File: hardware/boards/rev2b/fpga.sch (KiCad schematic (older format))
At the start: 71 parts, among them J1 SD_Card, J6 Conn_02x08_Odd_Even, Q1 DNP(RE1C002UN), SW1 SW_PUSH, U6 XC7A15T-FTG256, U7 MX25L3233F

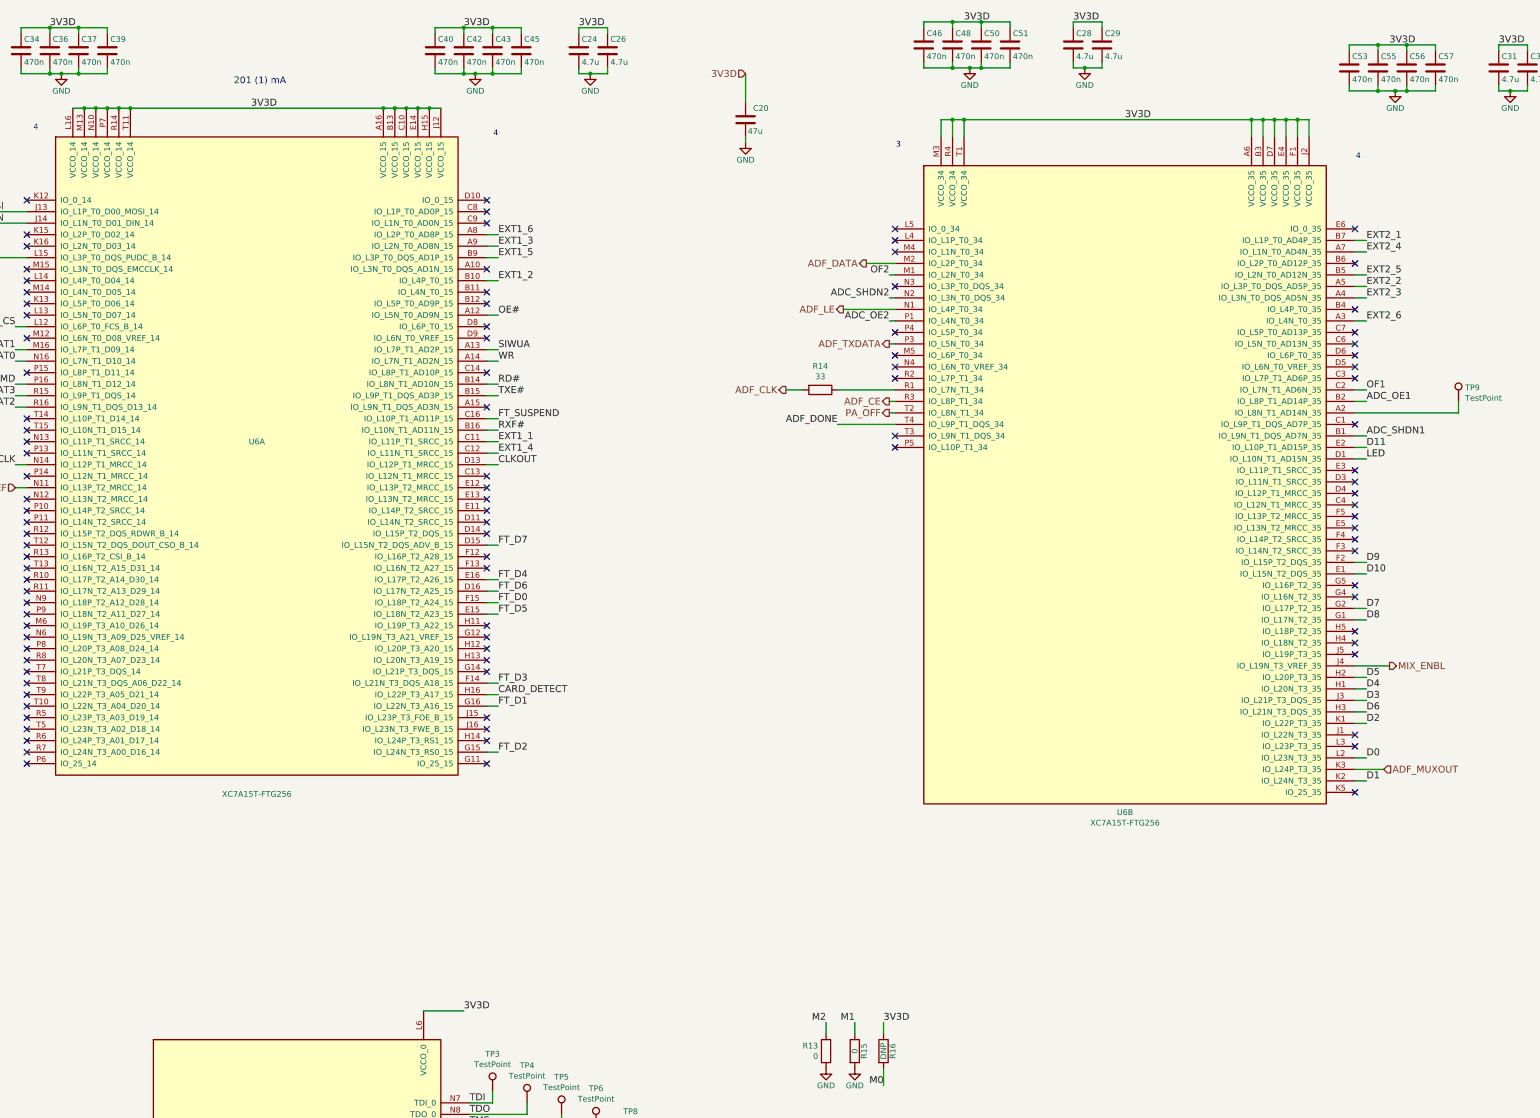
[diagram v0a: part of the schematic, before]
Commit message: rev2 pcb: finish routing traces
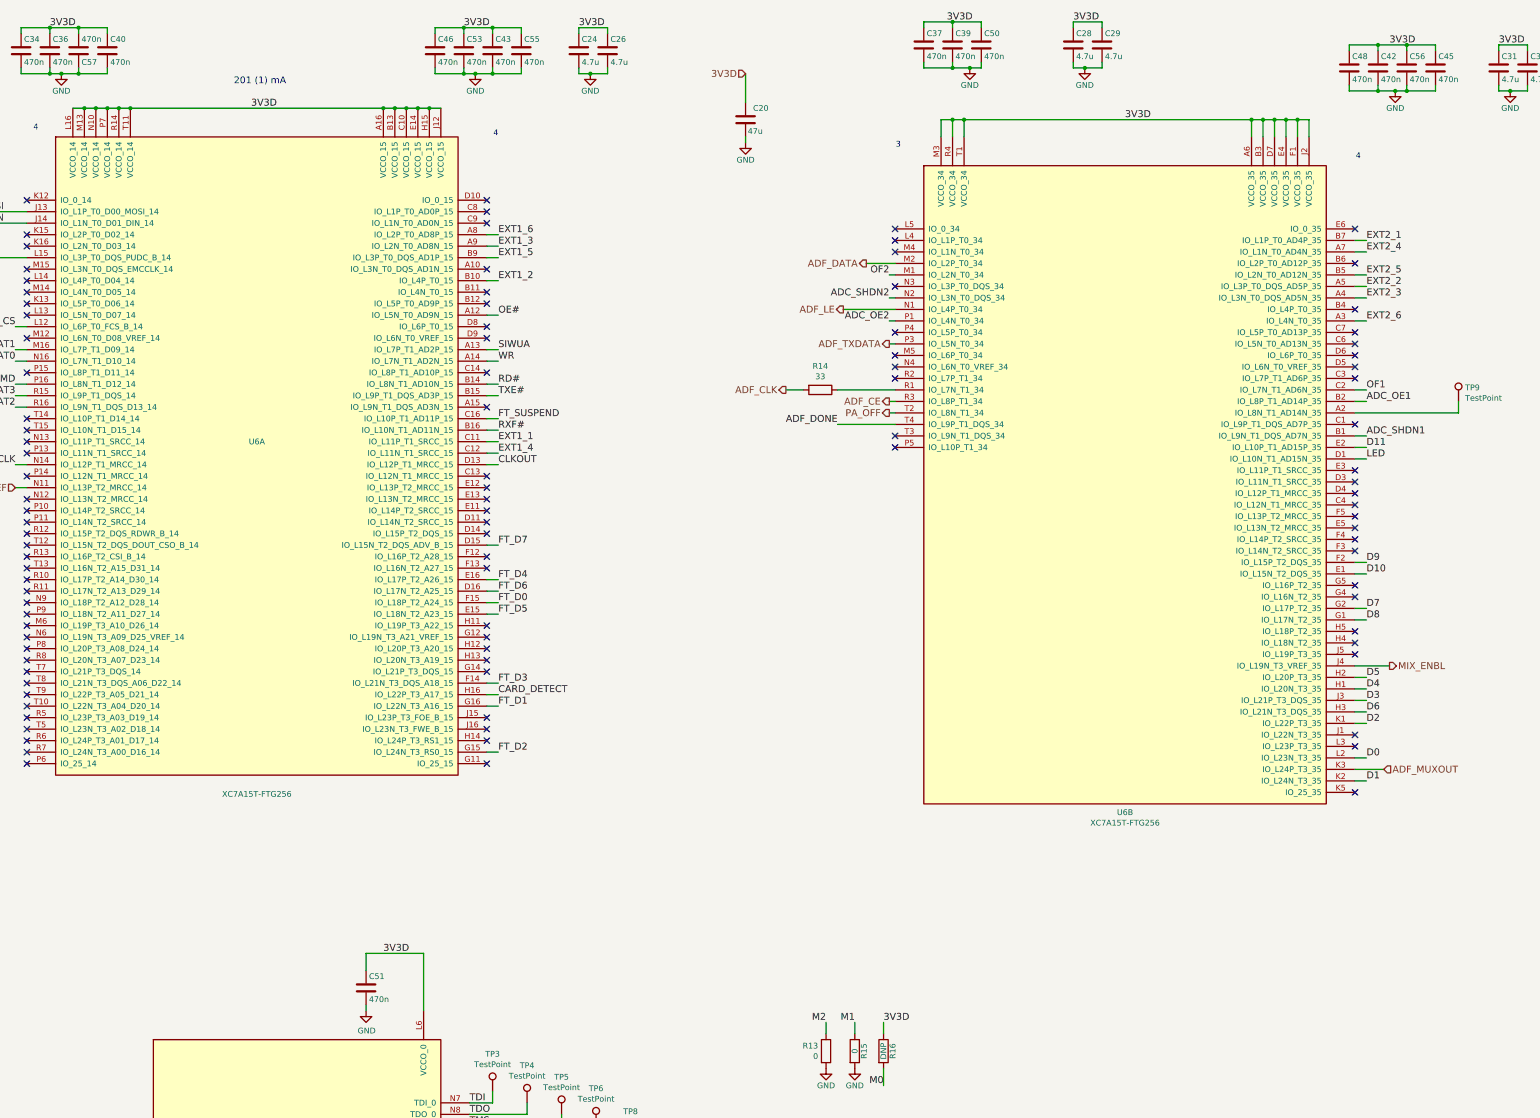
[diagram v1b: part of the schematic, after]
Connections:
- net 3V3D: now also C57.2; no longer C57.1
- net GND: now also C57.1; no longer C57.2
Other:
- moved on the sheet: C37, C39, C40, C42, C45, C46, C48, C51, C53, C55, C57
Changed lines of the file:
@@
 Connection ~ 19650 11900
 Connection ~ 16300 950
-Connection ~ 16550 950
 Connection ~ 20000 1150
 Connection ~ 20250 1150
 Connection ~ 20250 1550
 Connection ~ 20000 1550
-Connection ~ 16550 1350
 Connection ~ 16300 1350
 Connection ~ 7250 15300
@@
 	11150 14150 11150 14200
 Wire Wire Line
-	11700 9550 12050 9550
-Wire Wire Line
 	11800 1000 11800 1050
 Wire Wire Line
@@
 Wire Wire Line
 	16550 1350 16450 1350
-Wire Wire Line
-	16800 950  16550 950
-Wire Wire Line
-	16800 1000 16800 950
-Wire Wire Line
-	16800 1300 16800 1350
-Wire Wire Line
-	16800 1350 16550 1350
 Wire Wire Line
 	16850 11450 16850 11500
@@
 Text Label 12050 1000 0    60   ~ 0
 3V3D
-Text Label 12050 9550 0    60   ~ 0
+Text Label 11350 9050 0    60   ~ 0
 3V3D
 Text Label 12100 10350 0    60   ~ 0
@@
 Text Label 15750 3550 2    60   ~ 0
 ADC_OE2
-Text Label 16400 950  0    60   ~ 0
+Text Label 16250 950  0    60   ~ 0
 3V3D
 Text Label 16850 11450 0    60   ~ 0
@@
 L Device:C C37
 U 1 1 584FBF7D
-P 8700 1200
-F 0 "C37" H 8725 1300 50  0000 L CNN
-F 1 "470n" H 8725 1100 50  0000 L CNN
-F 2 "Capacitor_SMD:C_0603_1608Metric" H 8738 1050 30  0001 C CNN
-F 3 "" H 8700 1200 60  0000 C CNN
-F 4 "" H -3700 -6700 50  0001 C CNN "MFN"
-	1    8700 1200
+P 16050 1150
+F 0 "C37" H 16075 1250 50  0000 L CNN
+F 1 "470n" H 16075 1050 50  0000 L CNN
+F 2 "Capacitor_SMD:C_0603_1608Metric" H 16088 1000 30  0001 C CNN
+F 3 "" H 16050 1150 60  0000 C CNN
+F 4 "" H 3650 -6750 50  0001 C CNN "MFN"
+	1    16050 1150
 	1    0    0    -1
 $EndComp
@@
 L Device:C C39
 U 1 1 584FBE1F
-P 8950 1200
-F 0 "C39" H 8975 1300 50  0000 L CNN
-F 1 "470n" H 8975 1100 50  0000 L CNN
-F 2 "Capacitor_SMD:C_0603_1608Metric" H 8988 1050 30  0001 C CNN
-F 3 "" H 8950 1200 60  0000 C CNN
-F 4 "" H -3700 -6700 50  0001 C CNN "MFN"
-	1    8950 1200
+P 16300 1150
+F 0 "C39" H 16325 1250 50  0000 L CNN
+F 1 "470n" H 16325 1050 50  0000 L CNN
+F 2 "Capacitor_SMD:C_0603_1608Metric" H 16338 1000 30  0001 C CNN
+F 3 "" H 16300 1150 60  0000 C CNN
+F 4 "" H 3650 -6750 50  0001 C CNN "MFN"
+	1    16300 1150
 	1    0    0    -1
 $EndComp
@@
 L Device:C C40
 U 1 1 584FBCC6
-P 11800 1200
-F 0 "C40" H 11825 1300 50  0000 L CNN
-F 1 "470n" H 11825 1100 50  0000 L CNN
-F 2 "Capacitor_SMD:C_0603_1608Metric" H 11838 1050 30  0001 C CNN
-F 3 "" H 11800 1200 60  0000 C CNN
-F 4 "" H -1100 -6700 50  0001 C CNN "MFN"
-	1    11800 1200
+P 8950 1200
+F 0 "C40" H 8975 1300 50  0000 L CNN
+F 1 "470n" H 8975 1100 50  0000 L CNN
+F 2 "Capacitor_SMD:C_0603_1608Metric" H 8988 1050 30  0001 C CNN
+F 3 "" H 8950 1200 60  0000 C CNN
+F 4 "" H -3950 -6700 50  0001 C CNN "MFN"
+	1    8950 1200
 	1    0    0    -1
 $EndComp
@@
 L Device:C C42
 U 1 1 584FBB6A
-P 12050 1200
-F 0 "C42" H 12075 1300 50  0000 L CNN
-F 1 "470n" H 12075 1100 50  0000 L CNN
-F 2 "Capacitor_SMD:C_0603_1608Metric" H 12088 1050 30  0001 C CNN
-F 3 "" H 12050 1200 60  0000 C CNN
-F 4 "" H -1100 -6700 50  0001 C CNN "MFN"
-	1    12050 1200
+P 20000 1350
+F 0 "C42" H 20025 1450 50  0000 L CNN
+F 1 "470n" H 20025 1250 50  0000 L CNN
+F 2 "Capacitor_SMD:C_0603_1608Metric" H 20038 1200 30  0001 C CNN
+F 3 "" H 20000 1350 60  0000 C CNN
+F 4 "" H 6850 -6550 50  0001 C CNN "MFN"
+	1    20000 1350
 	1    0    0    -1
 $EndComp
@@
 L Device:C C45
 U 1 1 583B1CF1
-P 12550 1200
-F 0 "C45" H 12575 1300 50  0000 L CNN
-F 1 "470n" H 12575 1100 50  0000 L CNN
-F 2 "Capacitor_SMD:C_0603_1608Metric" H 12588 1050 30  0001 C CNN
-F 3 "" H 12550 1200 60  0000 C CNN
-F 4 "" H -1100 -6700 50  0001 C CNN "MFN"
-	1    12550 1200
+P 20500 1350
+F 0 "C45" H 20525 1450 50  0000 L CNN
+F 1 "470n" H 20525 1250 50  0000 L CNN
+F 2 "Capacitor_SMD:C_0603_1608Metric" H 20538 1200 30  0001 C CNN
+F 3 "" H 20500 1350 60  0000 C CNN
+F 4 "" H 6850 -6550 50  0001 C CNN "MFN"
+	1    20500 1350
 	1    0    0    -1
 $EndComp
@@
 L Device:C C46
 U 1 1 58531E80
-P 16050 1150
-F 0 "C46" H 16075 1250 50  0000 L CNN
-F 1 "470n" H 16075 1050 50  0000 L CNN
-F 2 "Capacitor_SMD:C_0603_1608Metric" H 16088 1000 30  0001 C CNN
-F 3 "" H 16050 1150 60  0000 C CNN
-F 4 "" H 2150 -6750 50  0001 C CNN "MFN"
-	1    16050 1150
+P 11800 1200
+F 0 "C46" H 11825 1300 50  0000 L CNN
+F 1 "470n" H 11825 1100 50  0000 L CNN
+F 2 "Capacitor_SMD:C_0603_1608Metric" H 11838 1050 30  0001 C CNN
+F 3 "" H 11800 1200 60  0000 C CNN
+F 4 "" H -2100 -6700 50  0001 C CNN "MFN"
+	1    11800 1200
 	1    0    0    -1
 $EndComp
@@
 L Device:C C48
 U 1 1 5C7E4CDC
-P 16300 1150
-F 0 "C48" H 16325 1250 50  0000 L CNN
-F 1 "470n" H 16325 1050 50  0000 L CNN
-F 2 "Capacitor_SMD:C_0603_1608Metric" H 16338 1000 30  0001 C CNN
-F 3 "" H 16300 1150 60  0000 C CNN
-F 4 "" H 2150 -6750 50  0001 C CNN "MFN"
-	1    16300 1150
+P 19750 1350
+F 0 "C48" H 19775 1450 50  0000 L CNN
+F 1 "470n" H 19775 1250 50  0000 L CNN
+F 2 "Capacitor_SMD:C_0603_1608Metric" H 19788 1200 30  0001 C CNN
+F 3 "" H 19750 1350 60  0000 C CNN
+F 4 "" H 5600 -6550 50  0001 C CNN "MFN"
+	1    19750 1350
 	1    0    0    -1
 $EndComp
@@
 L Device:C C51
 U 1 1 5C7E4E26
-P 16800 1150
-F 0 "C51" H 16825 1250 50  0000 L CNN
-F 1 "470n" H 16825 1050 50  0000 L CNN
-F 2 "Capacitor_SMD:C_0603_1608Metric" H 16838 1000 30  0001 C CNN
-F 3 "" H 16800 1150 60  0000 C CNN
-F 4 "" H 2150 -6750 50  0001 C CNN "MFN"
-	1    16800 1150
+P 11200 9350
+F 0 "C51" H 11225 9450 50  0000 L CNN
+F 1 "470n" H 11225 9250 50  0000 L CNN
+F 2 "Capacitor_SMD:C_0603_1608Metric" H 11238 9200 30  0001 C CNN
+F 3 "" H 11200 9350 60  0000 C CNN
+F 4 "" H -3450 1450 50  0001 C CNN "MFN"
+	1    11200 9350
 	1    0    0    -1
 $EndComp
@@
 L Device:C C53
 U 1 1 5C7E4ECC
-P 19750 1350
-F 0 "C53" H 19775 1450 50  0000 L CNN
-F 1 "470n" H 19775 1250 50  0000 L CNN
-F 2 "Capacitor_SMD:C_0603_1608Metric" H 19788 1200 30  0001 C CNN
-F 3 "" H 19750 1350 60  0000 C CNN
-F 4 "" H 4850 -6550 50  0001 C CNN "MFN"
-	1    19750 1350
+P 12050 1200
+F 0 "C53" H 12075 1300 50  0000 L CNN
+F 1 "470n" H 12075 1100 50  0000 L CNN
+F 2 "Capacitor_SMD:C_0603_1608Metric" H 12088 1050 30  0001 C CNN
+F 3 "" H 12050 1200 60  0000 C CNN
+F 4 "" H -2850 -6700 50  0001 C CNN "MFN"
+	1    12050 1200
 	1    0    0    -1
 $EndComp
@@
 L Device:C C55
 U 1 1 5C7E4F74
-P 20000 1350
-F 0 "C55" H 20025 1450 50  0000 L CNN
-F 1 "470n" H 20025 1250 50  0000 L CNN
-F 2 "Capacitor_SMD:C_0603_1608Metric" H 20038 1200 30  0001 C CNN
-F 3 "" H 20000 1350 60  0000 C CNN
-F 4 "" H 4850 -6550 50  0001 C CNN "MFN"
-	1    20000 1350
+P 12550 1200
+F 0 "C55" H 12575 1300 50  0000 L CNN
+F 1 "470n" H 12575 1100 50  0000 L CNN
+F 2 "Capacitor_SMD:C_0603_1608Metric" H 12588 1050 30  0001 C CNN
+F 3 "" H 12550 1200 60  0000 C CNN
+F 4 "" H -2600 -6700 50  0001 C CNN "MFN"
+	1    12550 1200
 	1    0    0    -1
 $EndComp
@@
 L Device:C C57
 U 1 1 5C7E50CE
-P 20500 1350
-F 0 "C57" H 20525 1450 50  0000 L CNN
-F 1 "470n" H 20525 1250 50  0000 L CNN
-F 2 "Capacitor_SMD:C_0603_1608Metric" H 20538 1200 30  0001 C CNN
-F 3 "" H 20500 1350 60  0000 C CNN
-F 4 "" H 4850 -6550 50  0001 C CNN "MFN"
-	1    20500 1350
-	1    0    0    -1
+P 8700 1200
+F 0 "C57" H 8725 1300 50  0000 L CNN
+F 1 "470n" H 8725 1100 50  0000 L CNN
+F 2 "Capacitor_SMD:C_0603_1608Metric" H 8738 1050 30  0001 C CNN
+F 3 "" H 8700 1200 60  0000 C CNN
+F 4 "" H -6950 -6700 50  0001 C CNN "MFN"
+	1    8700 1200
+	1    0    0    1
 $EndComp
 $Comp
@@
 	1    0    0    -1
 $EndComp
+Wire Wire Line
+	11700 9550 11700 9050
+Wire Wire Line
+	11700 9050 11200 9050
+Wire Wire Line
+	11200 9050 11200 9200
+Wire Wire Line
+	11200 9500 11200 9550
+$Comp
+L power:GND #PWR024
+U 1 1 5F83466E
+P 11200 9550
+F 0 "#PWR024" H 11200 9300 50  0001 C CNN
+F 1 "GND" H 11205 9377 50  0000 C CNN
+F 2 "" H 11200 9550 50  0001 C CNN
+F 3 "" H 11200 9550 50  0001 C CNN
+	1    11200 9550
+	1    0    0    -1
+$EndComp
